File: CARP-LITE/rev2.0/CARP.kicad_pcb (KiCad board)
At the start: 4 copper layers, 40 x 70.1 mm, 154 parts, among them J1 USB-C, J10 PYRO_2, J11 RF_L, J3 I2C1+3V3, J4 2S XT30, J5 UART+5V+I2C1, J6 PYRO_1, J7 RF_H, J8 PWM1+5V1, J9 PWM2+5V1, Q5 SQ2318CES, Q6 SQ2318CES, Q7 SQ2318CES, SW1 SW_Push, SW2 SW_Push, U1 W25Q128JVSIMTR (16MB), U10 TPS62130A, U2 W25Q32RVXHJQ (2MB), U4 RP2350_60QFN, U5 LSM6DSO, U6 BMP390, U7 TLV75733PDBV, U9 LR2021IMLTRT, Y1 ABM8-272-T3, Y2 ECS-TXO-25CSMV-320-AN-TR

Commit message: correct drc issues: flight data flash power and flipped resistor (doesnt matter but drc complained)
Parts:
- turned R16 to 0 degrees
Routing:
- net +3V3: track 27.8 -> 28.4 mm
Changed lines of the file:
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@@
 	(footprint "Resistor_SMD:R_0402_1005Metric"
 		(layer "F.Cu")
-		(at 443.05 282.7 180)
+		(at 443.05 282.7)
 		(descr "Resistor SMD 0402 (1005 Metric), square (rectangular) end terminal, IPC-7351 nominal, (Body size source: IPC-SM-782 page 72, https://www.pcb-3d.com/wordpress/wp-content/uploads/ipc-sm-782a_amendment_1_and_2.pdf)")
 		(tags "resistor")
 		(property "Reference" "R16"
-			(at 0.201 0.887 180)
+			(at -0.01 -0.86 0)
 			(layer "F.SilkS")
 			(effects
@@
 		)
 		(property "Value" "1k"
-			(at 0 1.17 180)
+			(at 0 1.17 0)
 			(layer "F.Fab")
 			(effects
@@
 		)
 		(property "Datasheet" ""
-			(at 0 0 180)
+			(at 0 0 0)
 			(layer "F.Fab")
 			(hide yes)
@@
 		)
 		(property "Description" ""
-			(at 0 0 180)
+			(at 0 0 0)
 			(layer "F.Fab")
 			(hide yes)
@@
 		)
 		(property "KiLib_Generator" "SMD_2terminal_chip_molded"
-			(at 0 0 180)
+			(at 0 0 0)
 			(layer "F.SilkS")
 			(hide yes)
@@
 		(duplicate_pad_numbers_are_jumpers no)
 		(fp_line
-			(start -0.153641 0.38)
-			(end 0.153641 0.38)
+			(start -0.153641 -0.38)
+			(end 0.153641 -0.38)
 			(stroke
 				(width 0.12)
@@
 		)
 		(fp_line
-			(start -0.153641 -0.38)
-			(end 0.153641 -0.38)
+			(start -0.153641 0.38)
+			(end 0.153641 0.38)
 			(stroke
 				(width 0.12)
@@
 		)
 		(fp_text user "${REFERENCE}"
-			(at 0 0 180)
+			(at 0 0 0)
 			(layer "F.Fab")
 			(effects
@@
 		)
 		(pad "1" smd roundrect
-			(at -0.51 0 180)
+			(at -0.51 0)
 			(size 0.54 0.64)
 			(layers "F.Cu" "F.Mask" "F.Paste")
@@
 		)
 		(pad "2" smd roundrect
-			(at 0.51 0 180)
+			(at 0.51 0)
 			(size 0.54 0.64)
 			(layers "F.Cu" "F.Mask" "F.Paste")
@@
 	)
 	(segment
+		(start 425.585 293.49)
+		(end 425.585 292.849999)
+		(width 0.8)
+		(layer "F.Cu")
+		(net "+3V3")
+	)
+	(segment
 		(start 441.25 302.0126)
 		(end 441.25 302.512399)
@@
 	)
 	(segment
+		(start 445.575 282.7)
+		(end 443.56 282.7)
+		(width 0.5)
+		(layer "F.Cu")
+		(net "+5V")
+	)
+	(segment
 		(start 436.2 259)
 		(end 433.7 261.5)
@@
 		(layer "F.Cu")
 		(net "+5V")
-	)
-	(segment
-		(start 445.575 282.7)
-		(end 443.875 282.7)
-		(width 0.5)
-		(layer "F.Cu")
-		(net "+5V")

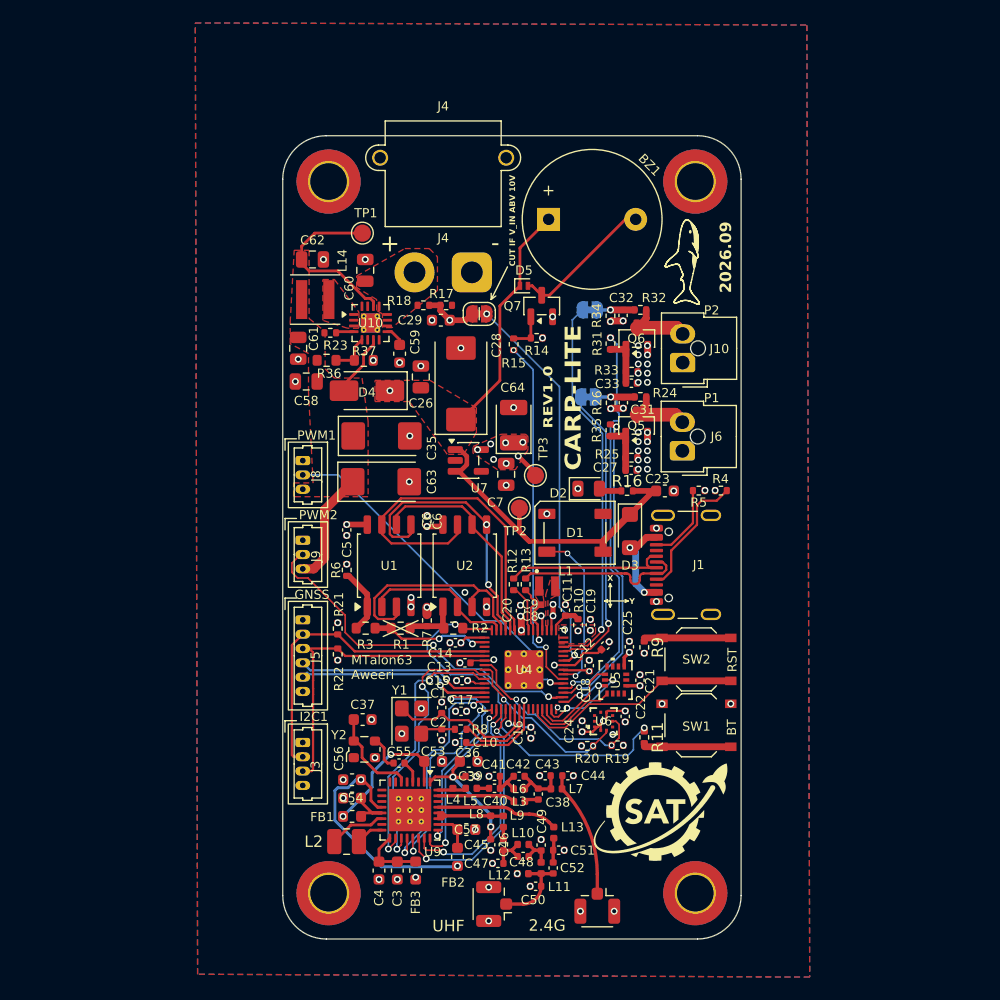
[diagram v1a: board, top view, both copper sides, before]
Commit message: flip pcb for better fullscreen ops
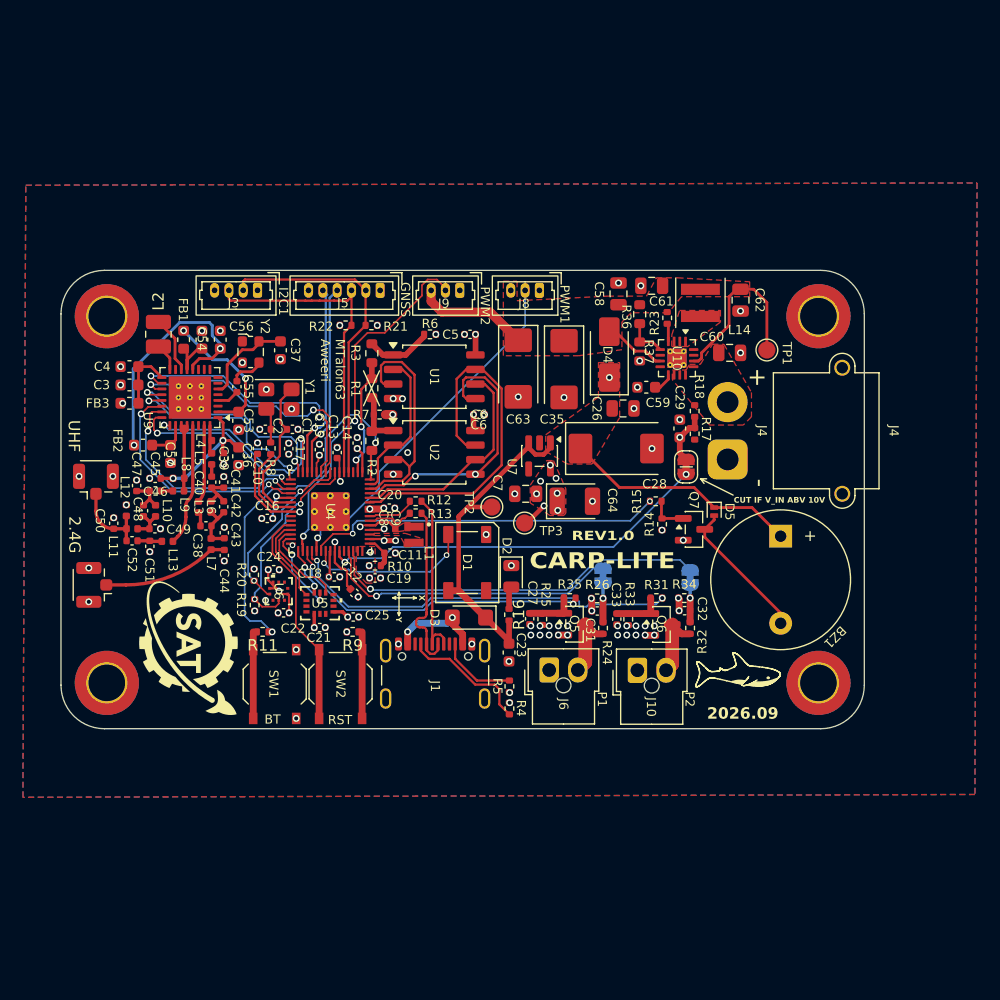
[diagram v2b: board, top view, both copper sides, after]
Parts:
- moved REF** 66.1 mm to (474.9, 302.5), turned to 0 degrees
- moved H4 54.5 mm to (397.6, 299.4), turned to -90 degrees
- moved H3 53.9 mm to (397.6, 267.4), turned to -90 degrees
- moved J7 52.7 mm to (396.1, 290.9), turned to 180 degrees
- moved J11 50.7 mm to (396.7, 281.4), turned to 90 degrees
- moved C4 49.1 mm to (399.6, 271.9), turned to 180 degrees
- moved C50 48.6 mm to (398.2, 285.5), turned to 90 degrees
- moved C3 48.4 mm to (399.6, 273.4), turned to 180 degrees
- moved FB3 47.8 mm to (399.6, 275.1), turned to 180 degrees
- moved L2 47.2 mm to (402.1, 269.0), turned to 90 degrees
- moved L12 46.9 mm to (399.4, 284.4), turned to 90 degrees
- moved C52 46.5 mm to (399.9, 287.1), turned to 0 degrees
- moved L11 46.4 mm to (399.9, 286.0), turned to 180 degrees
- moved C47 45.6 mm to (400.2, 282.2), turned to 90 degrees
- moved FB2 45.2 mm to (400.8, 278.7), turned to 0 degrees
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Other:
- board size 40 x 70.1 mm -> 70.1 x 40 mm
